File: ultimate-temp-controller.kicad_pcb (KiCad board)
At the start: 2 copper layers, 80 x 100 mm, 70 parts, among them CON1 SD_Card, IC1 ATMEGA328-A, P1 ISP, P10 RS485, P2 BUTTONS, P3 OPEN_DRAIN, P4 POWER, P5 I2C1, P6 I2C2, P7 CONN_01X05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

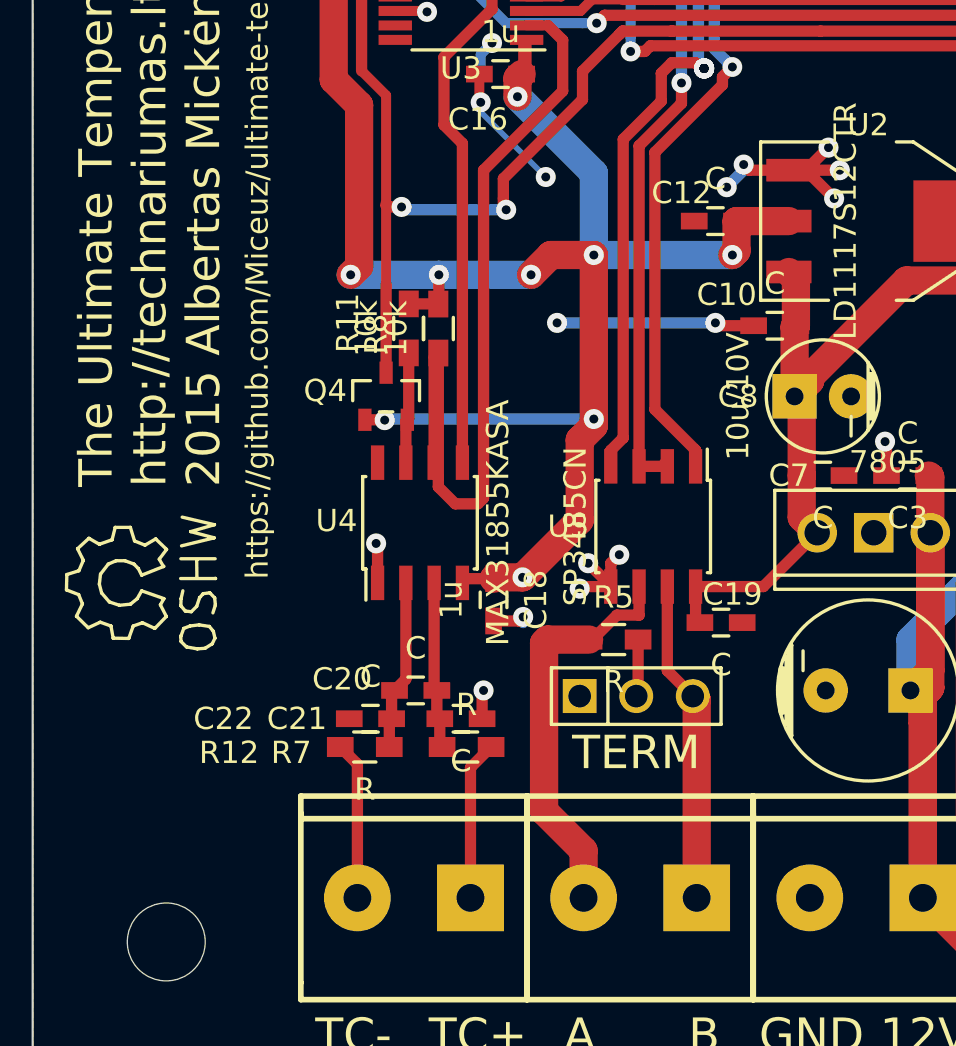
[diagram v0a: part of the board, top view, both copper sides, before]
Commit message: Add protection devices ot the PCB
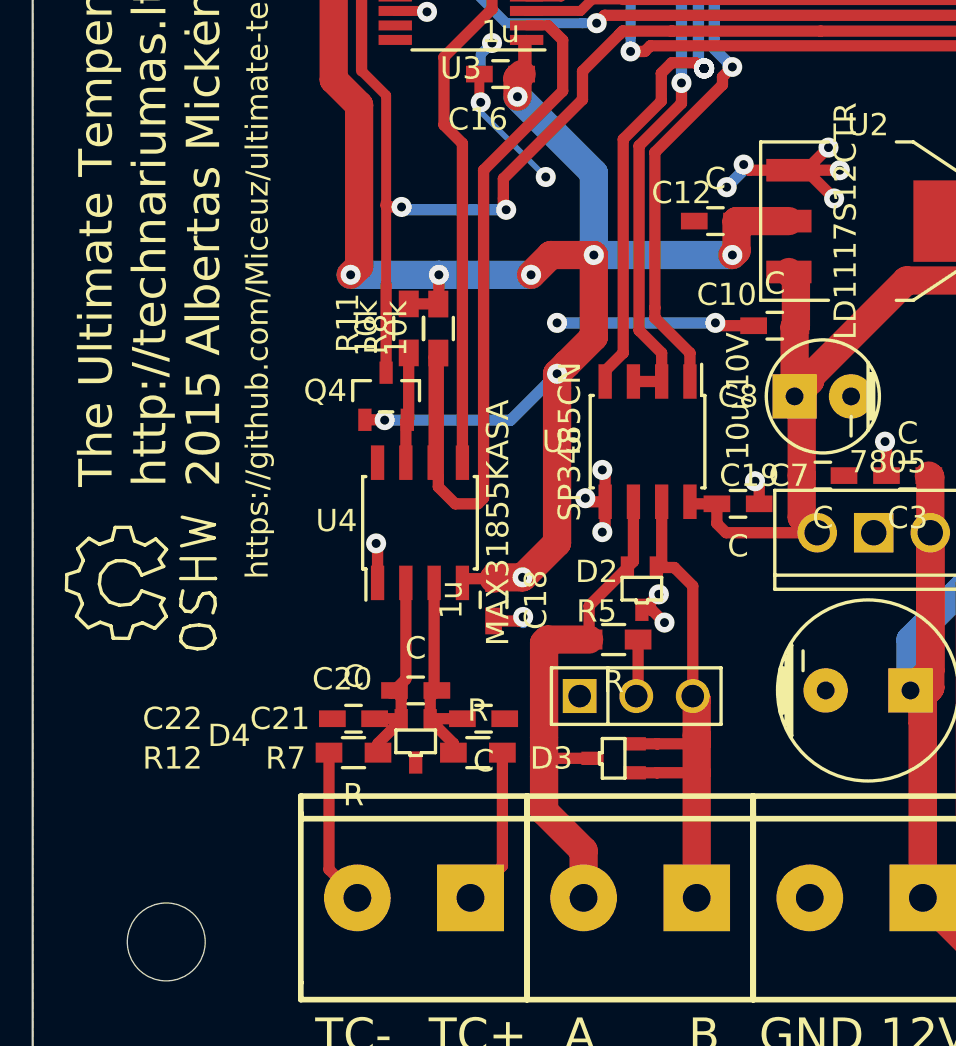
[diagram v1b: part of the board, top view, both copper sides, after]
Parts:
- added D2: TVS-DUAL, SMD_Packages:SOT-323, F.Cu at (118.4, 167.1)
- added D3: TVS-DUAL, SMD_Packages:SOT-323, F.Cu at (117.1, 174.8)
- added D4: TVS-DUAL, SMD_Packages:SOT-323, F.Cu at (108.2, 174.0)
- moved C19 5.39 mm to (122.7, 163.3)
- moved U5 3.82 mm to (118.6, 160.5)
- moved C21 1.02 mm to (111.3, 173.0)
- moved C22 0.76 mm to (105.4, 173.0)
- moved R12 0.57 mm to (105.4, 174.5)
- moved R7 0.57 mm to (111.0, 174.5)
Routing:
- net /controller/RS485B: track 14.8 -> 25.0 mm
- net /controller/RS485A: track 18.4 -> 23.8 mm
- net /controller/TXD: track 85.7 -> 81.6 mm
- net /controller/RXD: track 87.6 -> 83.6 mm
- net /controller/RS485DE: track 75.9 -> 72.3 mm
- net Net-(C20-Pad1): track 7.52 -> 9.71 mm
- net Net-(C20-Pad2): track 7.68 -> 9.80 mm
- net +5V: track 159.7 -> 158.1 mm
- net GND: track 76.4 -> 77.8 mm, vias 45 -> 47
- net +3V3: track 133.8 -> 133.0 mm
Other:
- board text removed: "TERM"

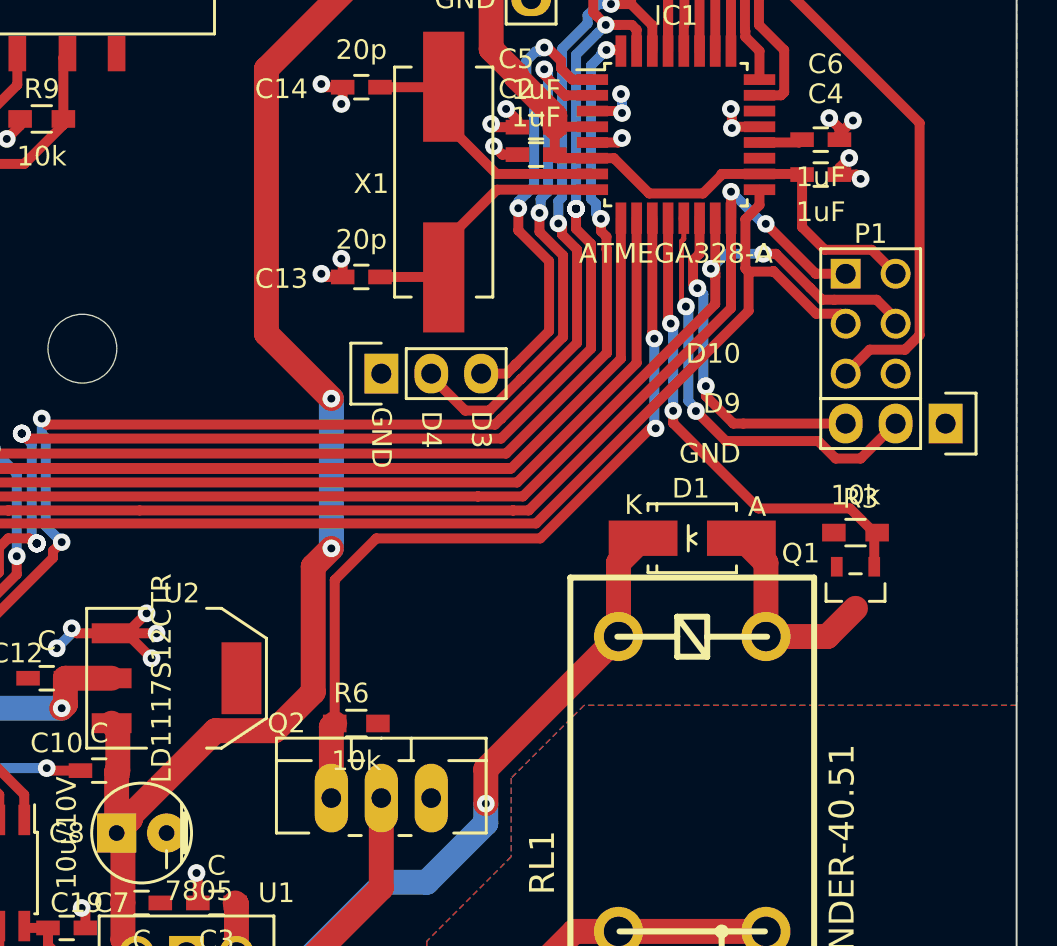
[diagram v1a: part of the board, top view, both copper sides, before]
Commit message: Consolidate spare pins on the expansion header
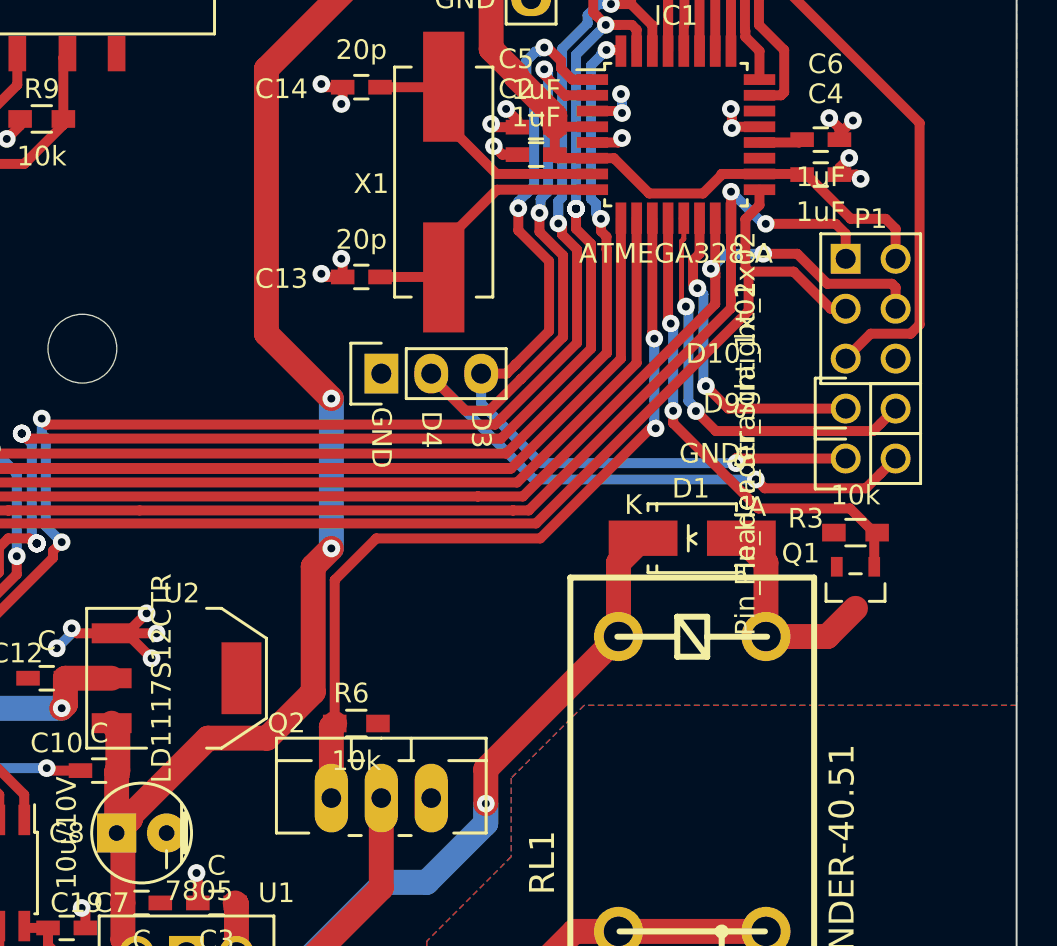
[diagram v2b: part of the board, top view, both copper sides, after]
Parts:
- removed the Pin_Header_Straight_1x03 at (167.4, 137.7)
- added Pin_Header_Straight_1x02: VAL**, Pin_Headers:Pin_Header_Straight_1x02, F.Cu at (162.3, 136.9)
- added Pin_Header_Straight_1x02: VAL**, Pin_Headers:Pin_Header_Straight_1x02, F.Cu at (162.3, 139.4)
- moved P1 0.76 mm to (163.6, 131.8)
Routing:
- net Net-(IC1-Pad2): track 26.8 -> 53.5 mm, vias 2 -> 3
- net Net-(IC1-Pad1): track 24.1 -> 45.7 mm, vias 2 -> 3
- net +5V: track 158.1 -> 157.1 mm
- net Net-(IC1-Pad13): track 22.1 -> 21.2 mm
- net /controller/RESET: track 54.0 -> 53.3 mm
- net Net-(IC1-Pad14): track 17.1 -> 16.5 mm

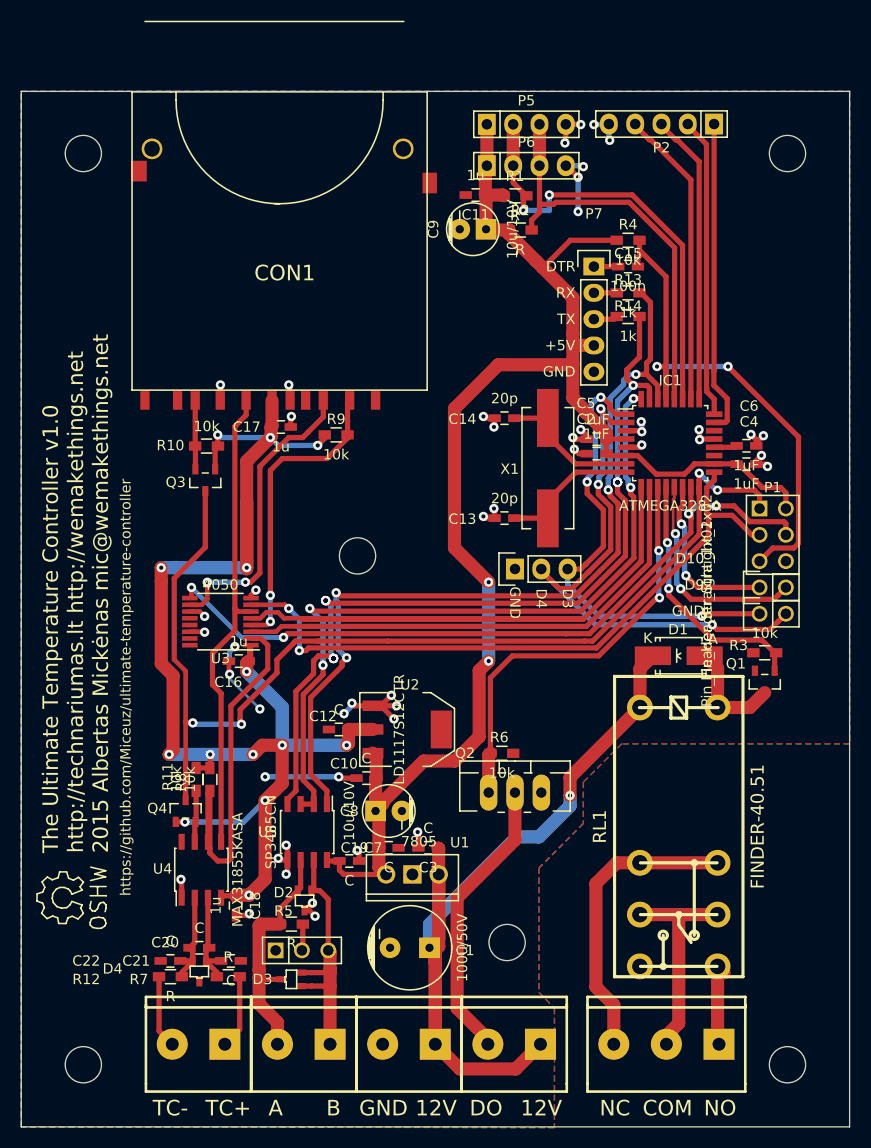
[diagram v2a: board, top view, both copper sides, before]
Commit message: Add comments about fixes for the next revision
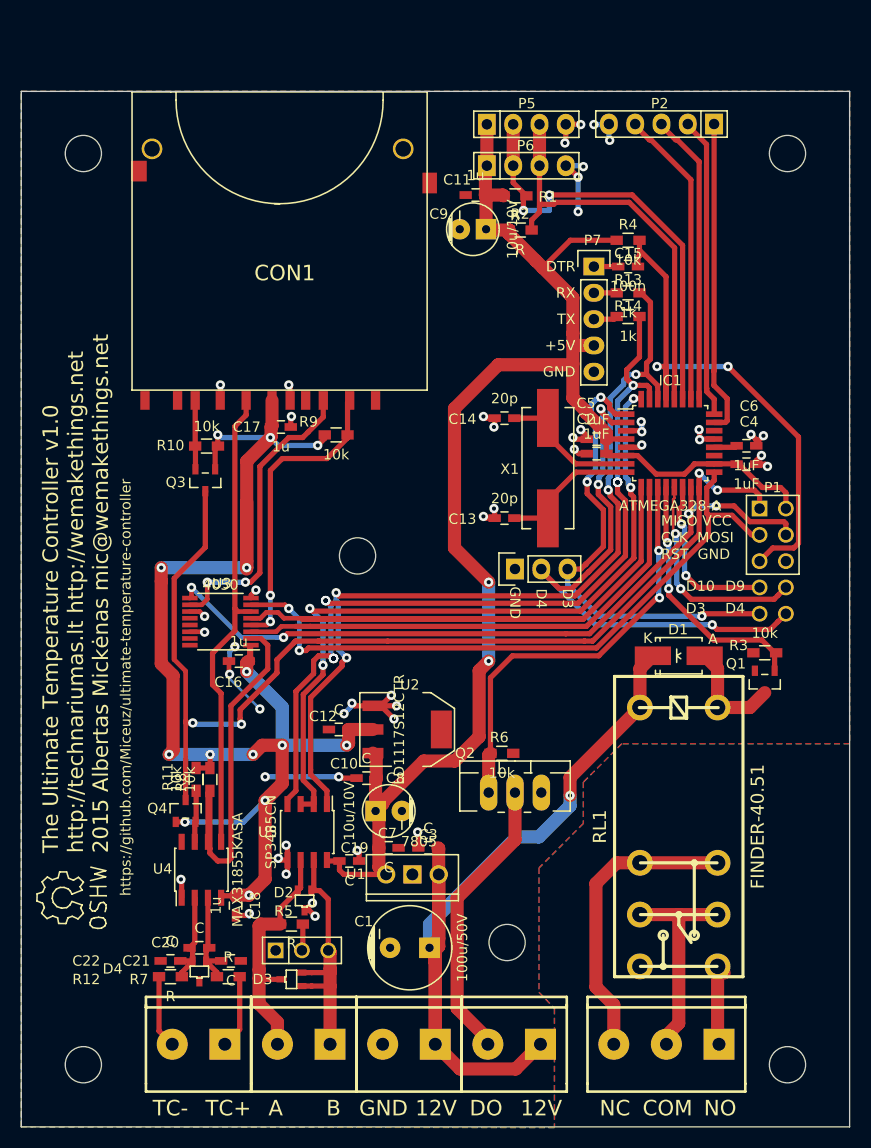
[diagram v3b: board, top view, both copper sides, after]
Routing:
- net +5V: track 157.1 -> 159.2 mm
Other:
- board text added: "MISO VCC CLK MOSI RST GND"
- board text added: "TODO: - SD korteles footprintas aukstyn kojom - TVS diodu footprintai SC-70, tuo tarpu, kai nusipirkau sot-23"

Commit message: Add more comments about what to fix
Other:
- board text added: "TODO: - SD korteles footprintas aukstyn kojom - TVS diodu footprintai SC-70, tuo tarpu, kai nusipirkau sot-23 - pakeist MCU i 328P, kad būtų arduino -rezistorių ant CLK ir MOSI linijų?"
- board text removed: "TODO: - SD korteles footprintas aukstyn kojom - TVS diodu footprintai SC-70, tuo tarpu, kai nusipirkau sot-23"

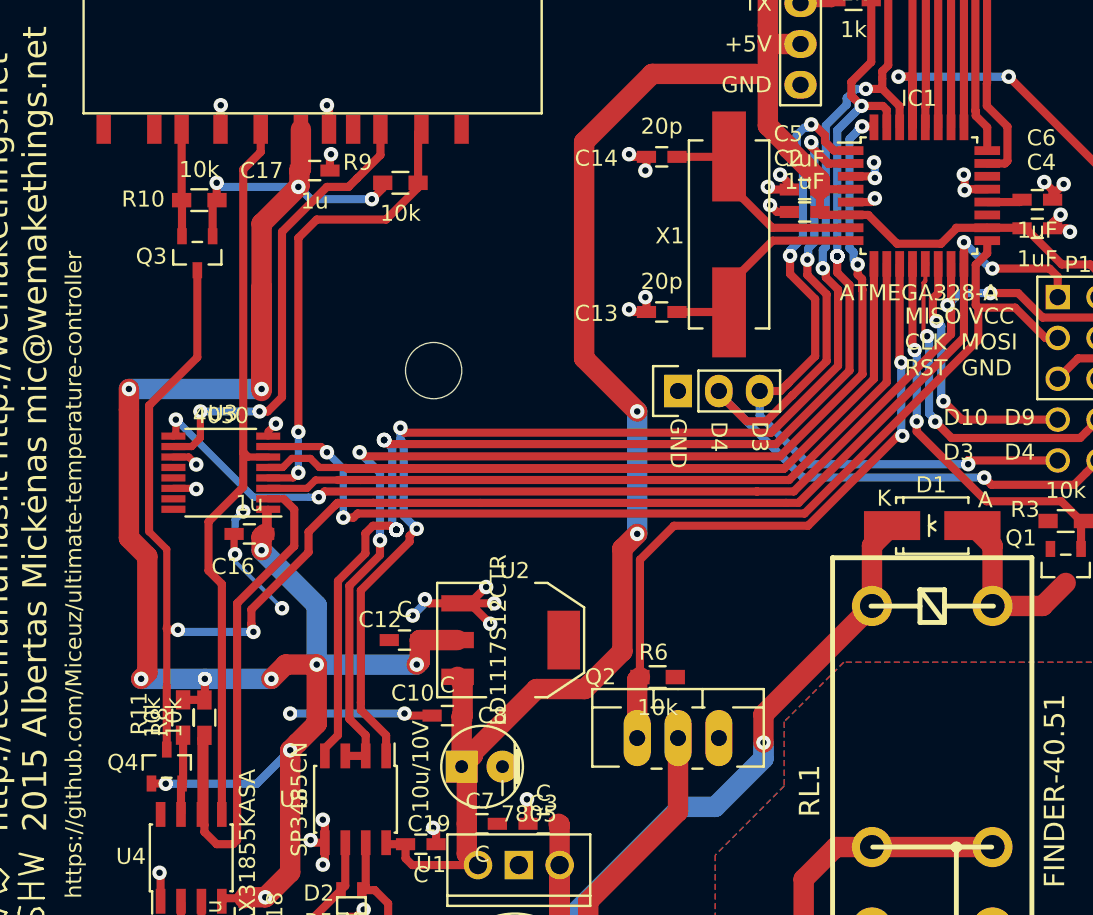
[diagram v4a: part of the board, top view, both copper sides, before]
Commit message: Fix SD card footprint by mirroring the pads
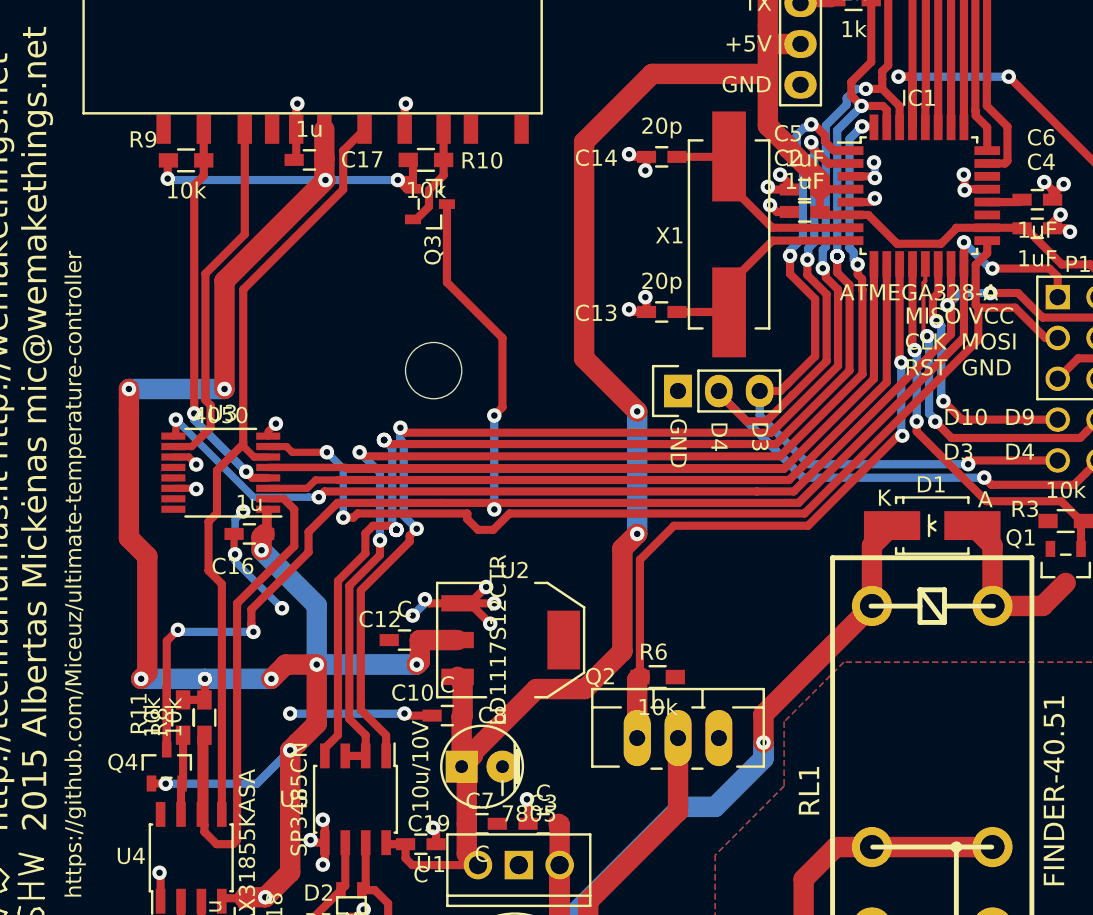
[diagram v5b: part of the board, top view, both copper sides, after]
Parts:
- moved Q3 14.8 mm to (123.2, 123.5), turned to 270 degrees
- moved R10 14.3 mm to (123.0, 120.8), turned to 0 degrees
- moved R9 13.4 mm to (108.1, 120.8)
- moved C17 0.74 mm to (115.8, 120.8), turned to 180 degrees
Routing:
- net /controller/MOSI_3V3: track 29.0 -> 22.5 mm, vias 2 -> 0
- net +3V3: track 133.0 -> 128.1 mm
- net /controller/CS_SD: track 74.9 -> 79.4 mm
- net /controller/CS_SD_3V3: track 29.2 -> 25.1 mm
- net /controller/CLK_3V3: track 46.0 -> 49.1 mm
- net GND: track 77.7 -> 78.8 mm, vias 47 -> 46
- net /controller/CLK: track 65.0 -> 66.0 mm
- net /controller/MISO: track 105.4 -> 105.9 mm, vias 4 -> 6
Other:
- board text added: "TODO: - TVS diodu footprintai SC-70, tuo tarpu, kai nusipirkau sot-23 - pakeist MCU i 328P, kad būtų arduino -rezistorių ant CLK ir MOSI linijų? - patikrinti SD kortelės footprintą"
- board text removed: "TODO: - SD korteles footprintas aukstyn kojom - TVS diodu footprintai SC-70, tuo tarpu, kai nusipirkau sot-23 - pakeist MCU i 328P, kad būtų arduino -rezistorių ant CLK ir MOSI linijų?"
